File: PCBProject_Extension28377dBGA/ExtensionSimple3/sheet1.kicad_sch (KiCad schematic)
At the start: 88 parts, among them J1 Conn_02x05_Odd_Even, J1 Conn_02x08_Top_Bottom, J2 Conn_01x02_Pin, Q1 FMMT618TA, U1 SN74ABT541, U2 SN74ABT541

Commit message: finish 7 commits
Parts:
- removed CAN1, CAN2, UART1, UART2, UART3, UART4: Conn_02x04_Counter_Clockwise, Connector_PinSocket_2.54mm:PinSocket_2x04_P2.54mm_Vertical, symbol Connector_Generic:Conn_02x04_Counter_Clockwise
- removed SPI-DAC: HIF3FC-20PA-2.54DSA, Connector_IDC:IDC-Header_2x10_P2.54mm_Vertical, symbol sheet1-altium-import:root_0_HIF3FC-20PA-2.54DSA
- added BiSS_C1, CAN_A1, CAN_B1: Conn_01x05, Connector_PinHeader_2.54mm:PinHeader_1x05_P2.54mm_Vertical, symbol Connector_Generic:Conn_01x05
- added C13, C16: 102, Capacitor_SMD:C_0805_2012Metric, symbol sheet1-altium-import:root_1_Cap
- added C14, C17: 102, Capacitor_SMD:C_0805_2012Metric, symbol sheet1-altium-import:root_0_Cap
- added C15, C18: 103, Capacitor_SMD:C_0805_2012Metric, symbol sheet1-altium-import:root_1_Cap
- added D4, D5: BAR43S, Package_TO_SOT_SMD:SOT-23, symbol sheet1-altium-import:root_1_BAR43S
- added J2 (x2): Conn_01x02_Pin, Connector_PinSocket_2.54mm:PinSocket_2x02_P2.54mm_Vertical, symbol Connector_Generic:Conn_02x02_Odd_Even
- added J6: Conn_02x05_Odd_Even, Connector_PinHeader_2.54mm:PinHeader_2x05_P2.54mm_Vertical, symbol Connector_Generic:Conn_02x05_Odd_Even
- added R34, R35, R39, R40, R44, R45: 10K, Resistor_SMD:R_0805_2012Metric, symbol sheet1-altium-import:root_2_Res2
- added R36, R41: 10K, Resistor_SMD:R_0805_2012Metric, symbol sheet1-altium-import:root_1_Res2
- added R37, R42: 10K, Resistor_SMD:R_0805_2012Metric, symbol sheet1-altium-import:root_0_Res2
- added R38, R43: 1K, Resistor_SMD:R_0805_2012Metric, symbol sheet1-altium-import:root_0_Res2
- added RU5: 0R, Resistor_SMD:R_0805_2012Metric, symbol sheet1-altium-import:root_0_Res2
- added SPI-DAC2: HIF3FC-20PA-2.54DSA, SamacSys_Parts:SHDR20W56P254_2X10_3290X850X950P, symbol sheet1-altium-import:root_0_HIF3FC-20PA-2.54DSA
- added UART1, UART2, UART3, UART4: Conn_01x06, Connector_PinHeader_2.54mm:PinHeader_1x06_P2.54mm_Vertical, symbol Connector_Generic:Conn_01x06
- added VDC_BUS3, VDC_BUS4: ${MANUFACTURER PART}, TestPoint:TestPoint_Pad_2.0x2.0mm, symbol sheet1-altium-import:root_1_TP-黄色测试点
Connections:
- net D12VGND is gone; now on net 12VGND: J1.13 (Pin_13), J1.13 (Pin_13), J1.15 (Pin_15), J1.15 (Pin_15)
- net MQEP2S is gone; now on net SPICLK: DSP1.27 (27_GP26)
- net MQEP2Z is gone; now on net AGND: DSP1.28 (GP27_28)
- net 12VGND: now also RU3.2
- net A+5V: now also R44.1, R45.1, SPI-DAC2.11, SPI-DAC2.12
- net A-5V: now also SPI-DAC2.10, SPI-DAC2.9
- net AGND: now also RU3.1, C13.1, C15.1, C16.1, C18.1, CAN_A1.3 (Pin_3), CAN_B1.3 (Pin_3), D4.1, D5.1, J2.1 (Pin_1), J2.1 (Pin_1), J2.3 (Pin_3), J2.3 (Pin_3), J6.10 (Pin_10), J6.3 (Pin_3), J6.4 (Pin_4), J6.9 (Pin_9), R35.2, R36.1, R40.2, R41.1, SPI-DAC2.5, SPI-DAC2.6, SPI-DAC2.7, SPI-DAC2.8, UART1.3 (Pin_3), UART2.3 (Pin_3), UART3.3 (Pin_3), UART4.3 (Pin_3)
- net AVDD: now also D4.2, D5.2
- net D+5V: now also SPI3.7 (Pin_7), SPI3.8 (Pin_8), CAN_A1.2 (Pin_2), CAN_B1.2 (Pin_2), SPI-DAC2.13, SPI-DAC2.14, UART1.1 (Pin_1), UART2.1 (Pin_1), UART3.1 (Pin_1), UART4.1 (Pin_1); no longer SPI3.3 (Pin_3), SPI3.4 (Pin_4)
- net D12V1: now also CAN_A1.1 (Pin_1), CAN_B1.1 (Pin_1)
- net DSP_A_CAN_RX: now also CAN_A1.4 (Pin_4)
- net DSP_A_CAN_TX: now also CAN_A1.5 (Pin_5)
- net DSP_B_CAN_RX: now also CAN_B1.4 (Pin_4)
- net DSP_B_CAN_TX: now also CAN_B1.5 (Pin_5)
- net IPM_VDC_BUS3: now also C18.2, D5.3, R43.2, VDC_BUS4.1
- net IPM_VDC_BUS4: now also C15.2, D4.3, R38.2, VDC_BUS3.1
- net PE_GND: now also SPI-DAC2.15, SPI-DAC2.16, SPI-DAC2.17, SPI-DAC2.18
- net REF_3V: now also J6.1 (Pin_1), J6.2 (Pin_2), RU5.1, UART1.2 (Pin_2), UART2.2 (Pin_2), UART3.2 (Pin_2), UART4.2 (Pin_2); no longer RU1.1, RU3.1
- net SPI_A_CK_HS: now also SPI3.4 (Pin_4)
- net SPI_A_MI_HS: now also SPI3.2 (Pin_2)
- net SPI_A_MO_HS: now also SPI3.1 (Pin_1)
- net SPI_B_CK_HS: no longer SPI3.7 (Pin_7)
- net SPI_B_MI_HS: no longer SPI3.2 (Pin_2)
- net SPI_B_MO_HS: no longer SPI3.1 (Pin_1)
- net SPI_C_CK_HS: now also SPI-DAC2.2
- net SPI_C_MI_HS: now also SPI-DAC2.4
- net SPI_C_MO_HS: now also SPI-DAC2.1
- net UART_SCI_RXDA: now also UART1.4 (Pin_4)
- net UART_SCI_RXDB: now also UART2.4 (Pin_4)
- net UART_SCI_RXDC: now also UART3.4 (Pin_4)
- net UART_SCI_RXDD: now also UART4.4 (Pin_4)
- net UART_SCI_TXDA: now also UART1.6 (Pin_6)
- net UART_SCI_TXDB: now also UART2.6 (Pin_6)
- net UART_SCI_TXDC: now also UART3.6 (Pin_6)
- net UART_SCI_TXDD: now also UART4.6 (Pin_6)
- net UART_SCI_WRA: now also UART1.5 (Pin_5)
- net UART_SCI_WRB: now also UART2.5 (Pin_5)
- net UART_SCI_WRC: now also UART3.5 (Pin_5)
- net UART_SCI_WRD: now also UART4.5 (Pin_5)
- net ~{SPI_A_STE_HS}: now also SPI3.3 (Pin_3)
- net ~{SPI_B_STE_HS}: no longer SPI3.8 (Pin_8)
- net ~{SPI_C_STE_HS}: now also SPI-DAC2.3
- net at N1.10: now also C16.2, R40.1, R41.2
- net at N1.8: now also C17.2, R42.2, R43.1
- net at N1.9: now also C17.1, R39.1, R42.1
- net TX_DIR: now reaches DSP1.124 (CS2_124)
- net TX_DIR: now also BiSS_C1.1 (Pin_1)
- net MSCLA: now reaches DSP1.149 (149_GP1)
- net MSCLA: now also J6.5 (Pin_5), J6.6 (Pin_6)
- net MSDAA: now reaches DSP1.150 (GP0_150)
- net MSDAA: now also J6.7 (Pin_7), J6.8 (Pin_8)
- net SPICLK: now reaches DSP1.38 (GP7_38)
- net SPICLK: now also BiSS_C1.5 (Pin_5)
- net at N1.12: now also C13.2, R35.1, R36.2
- net at N1.13: now also C14.1, R34.1, R37.1
- net at N1.14: now also C14.2, R37.2, R38.1
- net MQEP2A renamed DATA_IN
- net DATA_IN: now also BiSS_C1.2 (Pin_2)
- net MQEP2B renamed DATA_OUT
- net DATA_OUT: now also BiSS_C1.3 (Pin_3)
- net QEP2_HALL_V renamed PWR_CTL
- net PWR_CTL: now also BiSS_C1.4 (Pin_4)
- new net: RU5.2, SPI-DAC2.19, SPI-DAC2.20
- new net GND_2M3: J2.2 (Pin_2), J2.4 (Pin_4), R39.2, R45.2
- new net GND_2M4: J2.2 (Pin_2), J2.4 (Pin_4), R34.2, R44.2
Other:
- note added: "I2C"
- note added: "SPI_A for communication of DSPs"
- moved on the sheet: N1C, N1D, SPI3

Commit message: let VDD to 485
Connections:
- net REF_3V: no longer J6.1 (Pin_1), J6.2 (Pin_2), UART1.2 (Pin_2), UART2.2 (Pin_2), UART3.2 (Pin_2), UART4.2 (Pin_2)
- net VDD: now also J6.1 (Pin_1), J6.2 (Pin_2), UART1.2 (Pin_2), UART2.2 (Pin_2), UART3.2 (Pin_2), UART4.2 (Pin_2)

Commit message: fix VDD and ref_3V, DC_bus location
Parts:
- added TESTPOINT1, TESTPOINT2, TESTPOINT3, TESTPOINT4, TESTPOINT5, TESTPOINT6, TESTPOINT7: ${MANUFACTURER PART}, TestPoint:TestPoint_Pad_2.0x2.0mm, symbol sheet1-altium-import:root_1_TP-黄色测试点
- renumbered VDC_BUS4 to ANALOGINPUT1, VDC_BUS3 to ANALOGINPUT2, BiSS_C1 to CLB_BiSS_C1
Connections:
- net AGND: now also TESTPOINT3.1
- net DSP_A_CAN_RX: now also TESTPOINT6.1
- net DSP_A_CAN_TX: now also TESTPOINT7.1
- net SPI_C_CK_HS: now also TESTPOINT4.1
- net UART_SCI_RXDA: now also TESTPOINT1.1
- net UART_SCI_TXDA: now also TESTPOINT2.1
- net UART_SCI_WRA: now also TESTPOINT5.1
- net DATA_IN renamed CLB_DATA_IN
- net DATA_OUT renamed CLB_DATA_OUT
- net GND_2M3: no longer names the net of J2.2 (Pin_2), J2.4 (Pin_4), R39.2, R45.2
- net GND_2M4: no longer names the net of J2.2 (Pin_2), J2.4 (Pin_4), R34.2, R44.2
- net IPM_VDC_BUS3 renamed ANALOGINPUT1
- net IPM_VDC_BUS4 renamed ANALOGINPUT2
- net PWR_CTL renamed CLB_PWR_CTL
- net SPICLK renamed CLB_SPICLK
- net TX_DIR renamed CLB_TX_DIR
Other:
- moved on the sheet: ANALOGINPUT1, ANALOGINPUT2, J2, R34, R35, R40, R44, R45

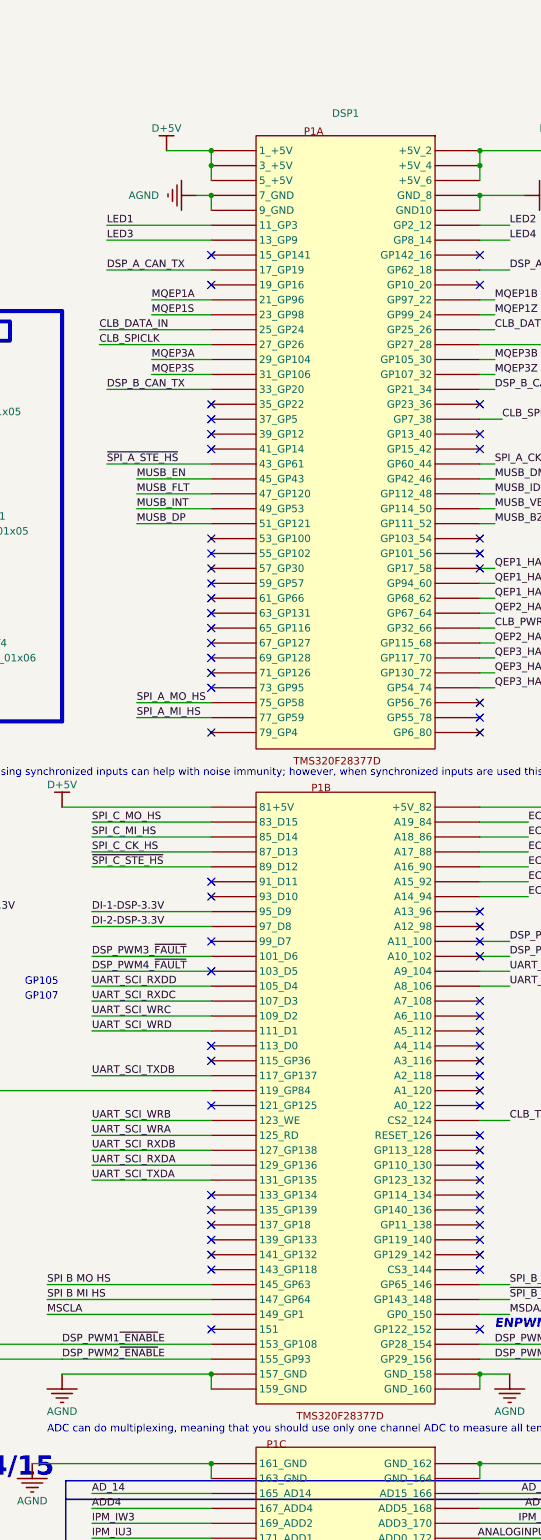
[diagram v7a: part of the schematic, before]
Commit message: Divide DSP, and Matched DC bus Net Lengths
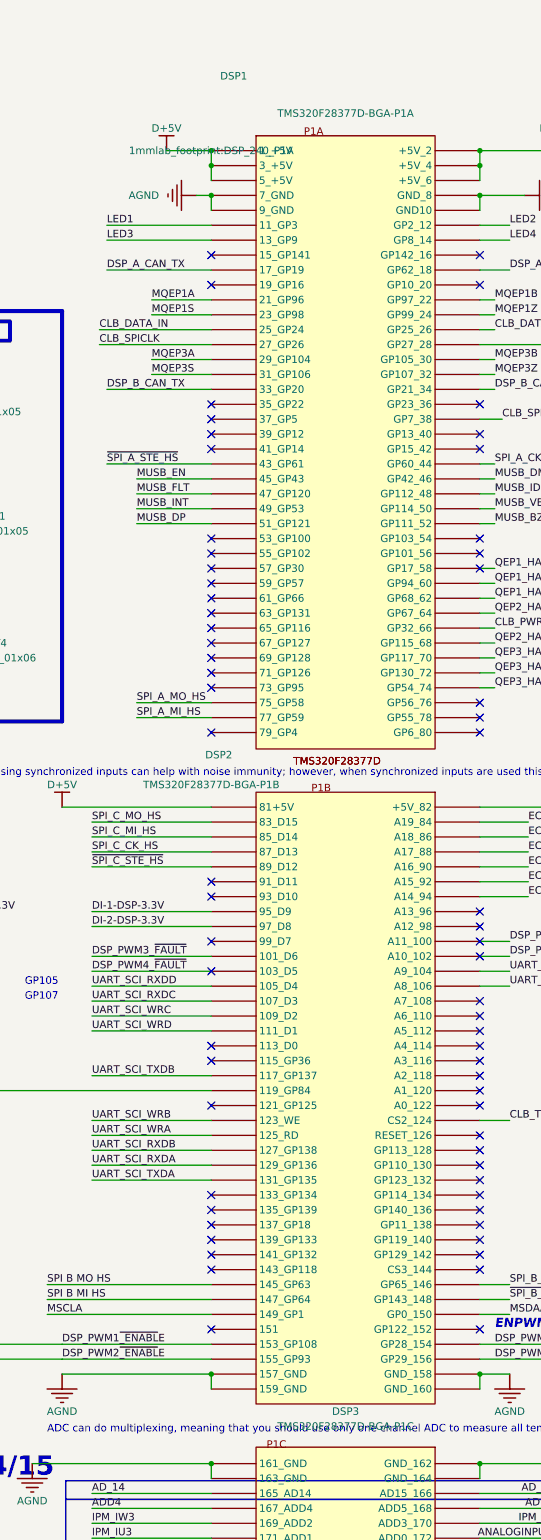
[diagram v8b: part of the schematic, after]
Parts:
- removed DSP1: ~, 1mmlab_footprint:DSP_240_SMD, symbol 1mmlab:TMS320F28377D-BGA-Core
- added DSP1: TMS320F28377D-BGA-P1A, 1mmlab_footprint:DSP_240_P1A, symbol 1mmlab:TMS320F28377D-BGA-P1A
- added DSP2: TMS320F28377D-BGA-P1B, 1mmlab_footprint:DSP_240_P1B, symbol 1mmlab:TMS320F28377D-BGA-P1B
- added DSP3: TMS320F28377D-BGA-P1C, 1mmlab_footprint:DSP_240_P1C, symbol 1mmlab:TMS320F28377D-BGA-P1C
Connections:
- net ADD4: now also DSP3.167 (167_ADD4)
- net ADD5: now also DSP3.168 (ADD5_168)
- net AD_14: now also DSP3.165 (165_AD14)
- net AD_15: now also DSP3.166 (AD15_166)
- net AGND: now also DSP1.10 (GND10), DSP1.28 (GP27_28), DSP1.7 (7_GND), DSP1.8 (GND_8), DSP1.9 (9_GND), DSP2.157 (157_GND), DSP2.158 (GND_158), DSP2.159 (159_GND), DSP2.160 (GND_160), DSP3.161 (161_GND), DSP3.162 (GND_162), DSP3.163 (163_GND), DSP3.164 (GND_164), DSP3.189 (189_GND), DSP3.190 (GND_190), DSP3.191 (191_GND), DSP3.192 (GND_192), DSP3.217 (217_GND), DSP3.218 (GND_218), DSP3.219 (219_GND), DSP3.220 (GND_220)
- net ANALOGINPUT1: now also DSP3.172 (ADD0_172)
- net ANALOGINPUT2: now also DSP3.176 (ADC2_176)
- net BootFromFlash: now also DSP2.119 (119_GP84)
- net CLB_DATA_IN: now also DSP1.25 (25_GP24)
- net CLB_DATA_OUT: now also DSP1.26 (GP25_26)
- net CLB_PWR_CTL: now also DSP1.66 (GP32_66)
- net CLB_SPICLK: now also DSP1.27 (27_GP26), DSP1.38 (GP7_38)
- net CLB_TX_DIR: now also DSP2.124 (CS2_124)
- net D+5V: now also DSP1.1 (1_+5V), DSP1.2 (+5V_2), DSP1.3 (3_+5V), DSP1.4 (+5V_4), DSP1.5 (5_+5V), DSP1.6 (+5V_6), DSP2.81 (81+5V), DSP2.82 (+5V_82)
- net DI-1-DSP-3.3V: now also DSP2.95 (95_D9)
- net DI-2-DSP-3.3V: now also DSP2.97 (97_D8)
- net DSP-PWM10A: now also DSP3.206 (PWM10A_206)
- net DSP-PWM10B: now also DSP3.208 (PWM10B_208)
- net DSP-PWM11A: now also DSP3.210 (PWM11A_210)
- net DSP-PWM11B: now also DSP3.212 (PWM11B_212)
- net DSP-PWM12A: now also DSP3.214 (PWM12A_214)
- net DSP-PWM12B: now also DSP3.216 (PWM12B_216)
- net DSP-PWM1A: now also DSP3.193 (193_PWM1A)
- net DSP-PWM1B: now also DSP3.195 (195_PWM1B)
- net DSP-PWM2A: now also DSP3.197 (197_PWM2A)
- net DSP-PWM2B: now also DSP3.199 (199_PWM2B)
- net DSP-PWM3A: now also DSP3.201 (201_PWM3A)
- net DSP-PWM3B: now also DSP3.203 (203_PWM3B)
- net DSP-PWM4A: now also DSP3.205 (205_PWM4A)
- net DSP-PWM4B: now also DSP3.207 (207_PWM4B)
- net DSP-PWM5A: now also DSP3.209 (209_PWM5A)
- net DSP-PWM5B: now also DSP3.211 (211_PWM5B)
- net DSP-PWM6A: now also DSP3.213 (213_PWM6A)
- net DSP-PWM6B: now also DSP3.215 (215_PWM6B)
- net DSP-PWM7A: now also DSP3.194 (PWM7A_194)
- net DSP-PWM7B: now also DSP3.196 (PWM7B_196)
- net DSP-PWM8A: now also DSP3.198 (PWM8A_198)
- net DSP-PWM8B: now also DSP3.200 (PWM8B_200)
- net DSP-PWM9A: now also DSP3.202 (PWM9A_202)
- net DSP-PWM9B: now also DSP3.204 (PWM9B_204)
- net DSP_A_CAN_RX: now also DSP1.18 (GP62_18)
- net DSP_A_CAN_TX: now also DSP1.17 (17_GP19)
- net DSP_B_CAN_RX: now also DSP1.34 (GP21_34)
- net DSP_B_CAN_TX: now also DSP1.33 (33_GP20)
- net DSP_PWM1_~{FAULT}: now also DSP2.102 (A10_102)
- net DSP_PWM1~{_ENABL}E: now also DSP2.153 (153_GP108)
- net DSP_PWM2_~{FAULT}: now also DSP2.100 (A11_100)
- net DSP_PWM2~{_ENABL}E: now also DSP2.155 (155_GP93)
- net DSP_PWM3_~{FAULT}: now also DSP2.101 (101_D6)
- net DSP_PWM3~{_ENABL}E: now also DSP2.154 (GP28_154)
- net DSP_PWM4_~{FAULT}: now also DSP2.103 (103_D5)
- net DSP_PWM4~{_ENABL}E: now also DSP2.156 (GP29_156)
- net ECAP1_IPM_TerminalDutyU1: now also DSP2.84 (A19_84)
- net ECAP2_IPM_TerminalDutyV1: now also DSP2.86 (A18_86)
- net ECAP3_IPM_TerminalDutyW1: now also DSP2.88 (A17_88)
- net ECAP4_IPM_TerminalDutyU2: now also DSP2.90 (A16_90)
- net ECAP5_IPM_TerminalDutyV2: now also DSP2.92 (A15_92)
- net ECAP6_IPM_TerminalDutyW2: now also DSP2.94 (A14_94)
- net IPM_IU1: now also DSP3.187 (187_ADA1)
- net IPM_IU2: now also DSP3.181 (181_ADB1)
- net IPM_IU3: now also DSP3.171 (171_ADD1)
- net IPM_IU4: now also DSP3.175 (175_ADC3)
- net IPM_IV1: now also DSP3.186 (ADA2_186)
- net IPM_IV2: now also DSP3.180 (ADB2_180)
- net IPM_IV3: now also DSP3.170 (ADD3_170)
- net IPM_IV4: now also DSP3.174 (ADC4_174)
- net IPM_IW1: now also DSP3.185 (185_ADA3)
- net IPM_IW2: now also DSP3.179 (179_ADB3)
- net IPM_IW3: now also DSP3.169 (169_ADD2)
- net IPM_IW4: now also DSP3.173 (173_ADC5)
- net IPM_Temperature1: now also DSP3.183 (183_ADA5)
- net IPM_Temperature2: now also DSP3.177 (177_ADB5)
- net IPM_Temperature3: now also DSP3.184 (ADA4_184)
- net IPM_Temperature4: now also DSP3.178 (ADB4_178)
- net IPM_VDC_BUS1: now also DSP3.188 (ADA0_188)
- net IPM_VDC_BUS2: now also DSP3.182 (ADB0_182)
- net LED1: now also DSP1.11 (11_GP3)
- net LED2: now also DSP1.12 (GP2_12)
- net LED3: now also DSP1.13 (13_GP9)
- net LED4: now also DSP1.14 (GP8_14)
- net MQEP1A: now also DSP1.21 (21_GP96)
- net MQEP1B: now also DSP1.22 (GP97_22)
- net MQEP1S: now also DSP1.23 (23_GP98)
- net MQEP1Z: now also DSP1.24 (GP99_24)
- net MQEP3A: now also DSP1.29 (29_GP104)
- net MQEP3B: now also DSP1.30 (GP105_30)
- net MQEP3S: now also DSP1.31 (31_GP106)
- net MQEP3Z: now also DSP1.32 (GP107_32)
- net MSCLA: now also DSP2.149 (149_GP1)
- net MSDAA: now also DSP2.150 (GP0_150)
- net MUSB_BZ: now also DSP1.52 (GP111_52)
- net MUSB_DM: now also DSP1.46 (GP42_46)
- net MUSB_DP: now also DSP1.51 (51_GP121)
- net MUSB_EN: now also DSP1.45 (45_GP43)
- net MUSB_FLT: now also DSP1.47 (47_GP120)
- net MUSB_ID: now also DSP1.48 (GP112_48)
- net MUSB_INT: now also DSP1.49 (49_GP53)
- net MUSB_VB: now also DSP1.50 (GP114_50)
- net QEP1_HALL_U: now also DSP1.62 (GP68_62)
- net QEP1_HALL_V: now also DSP1.60 (GP94_60)
- net QEP1_HALL_W: now also DSP1.58 (GP17_58)
- net QEP2_HALL_U: now also DSP1.68 (GP115_68)
- net QEP2_HALL_W: now also DSP1.64 (GP67_64)
- net QEP3_HALL_U: now also DSP1.70 (GP117_70)
- net QEP3_HALL_V: now also DSP1.72 (GP130_72)
- net QEP3_HALL_W: now also DSP1.74 (GP54_74)
- net SPI B MI HS: now also DSP2.147 (147_GP64)
- net SPI B MO HS: now also DSP2.145 (145_GP63)
- net SPI_A_CK_HS: now also DSP1.44 (GP60_44)
- net SPI_A_MI_HS: now also DSP1.77 (77_GP59)
- net SPI_A_MO_HS: now also DSP1.75 (75_GP58)
- net SPI_B_CK_HS: now also DSP2.146 (GP65_146)
- net SPI_C_CK_HS: now also DSP2.87 (87_D13)
- net SPI_C_MI_HS: now also DSP2.85 (85_D14)
- net SPI_C_MO_HS: now also DSP2.83 (83_D15)
- net UART_SCI_RXDA: now also DSP2.129 (129_GP136)
- net UART_SCI_RXDB: now also DSP2.127 (127_GP138)
- net UART_SCI_RXDC: now also DSP2.107 (107_D3)
- net UART_SCI_RXDD: now also DSP2.105 (105_D4)
- net UART_SCI_TXDA: now also DSP2.131 (131_GP135)
- net UART_SCI_TXDB: now also DSP2.117 (117_GP137)
- net UART_SCI_TXDC: now also DSP2.106 (A8_106)
- net UART_SCI_TXDD: now also DSP2.104 (A9_104)
- net UART_SCI_WRA: now also DSP2.125 (125_RD)
- net UART_SCI_WRB: now also DSP2.123 (123_WE)
- net UART_SCI_WRC: now also DSP2.109 (109_D2)
- net UART_SCI_WRD: now also DSP2.111 (111_D1)
- net ~{SPI_A_STE_HS}: now also DSP1.43 (43_GP61)
- net ~{SPI_B_STE_HS}: now also DSP2.148 (GP143_148)
- net ~{SPI_C_STE_HS}: now also DSP2.89 (89_D12)
